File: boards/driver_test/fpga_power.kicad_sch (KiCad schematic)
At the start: 34 parts, among them J2 Barrel_Jack_Switch, J3 Conn_01x24, J4 Conn_01x24, Q4 IRF7413, U2 74LVC245, U3 JTE0624D05, U4 ADP151-3.3, U5 LTC4231-1, U6 74HC4514, U7 74LVC2G04

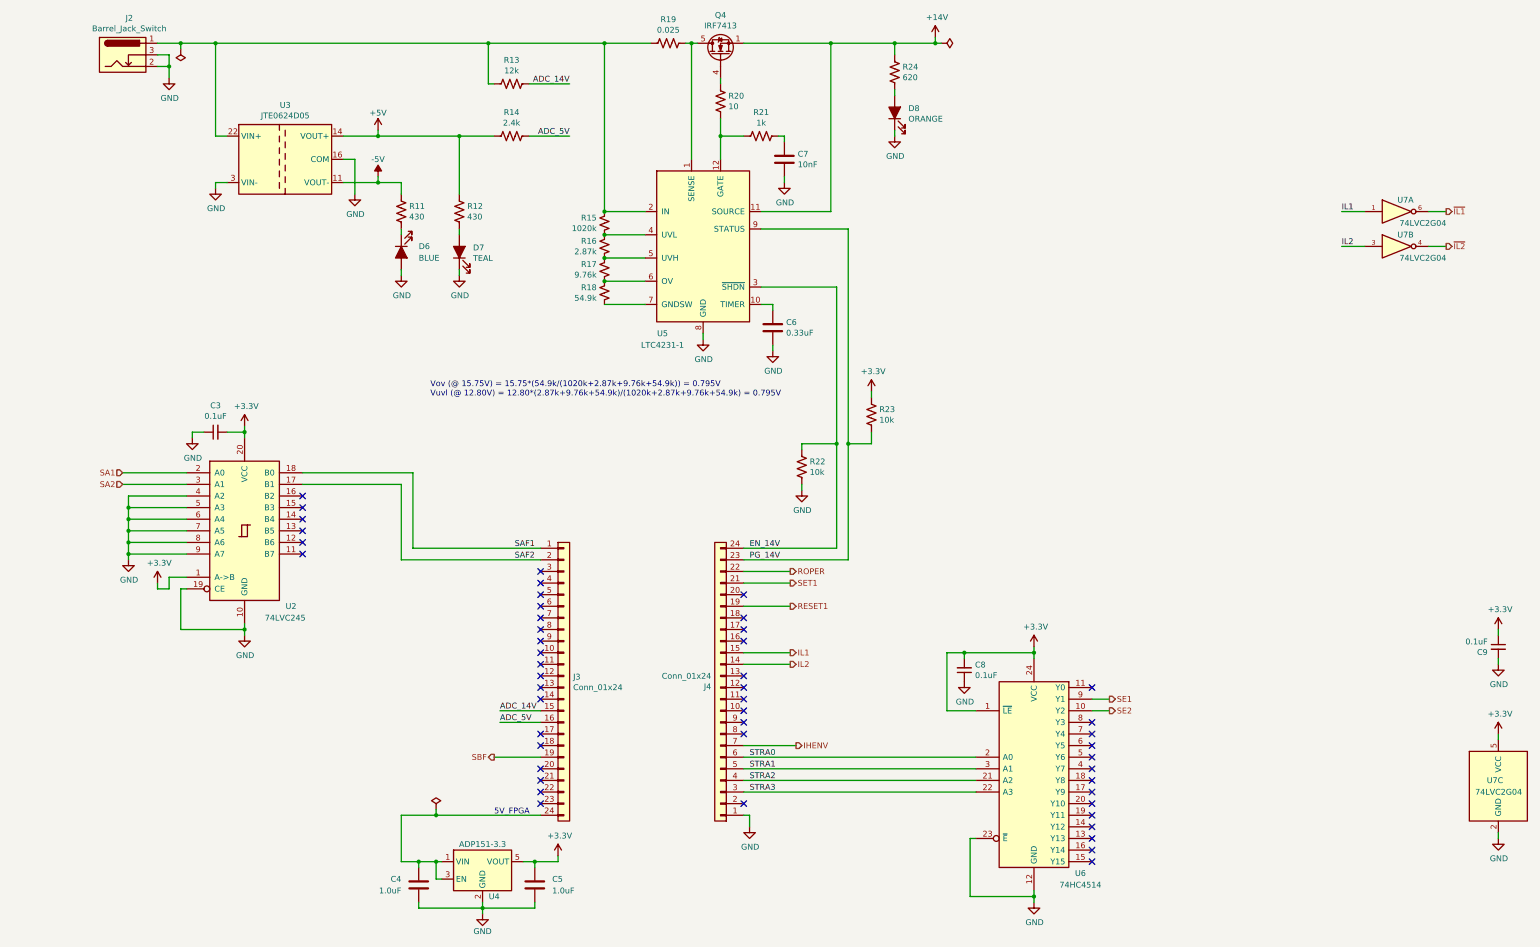
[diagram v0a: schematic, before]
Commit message: Driver test: completed much of the preliminary layout.
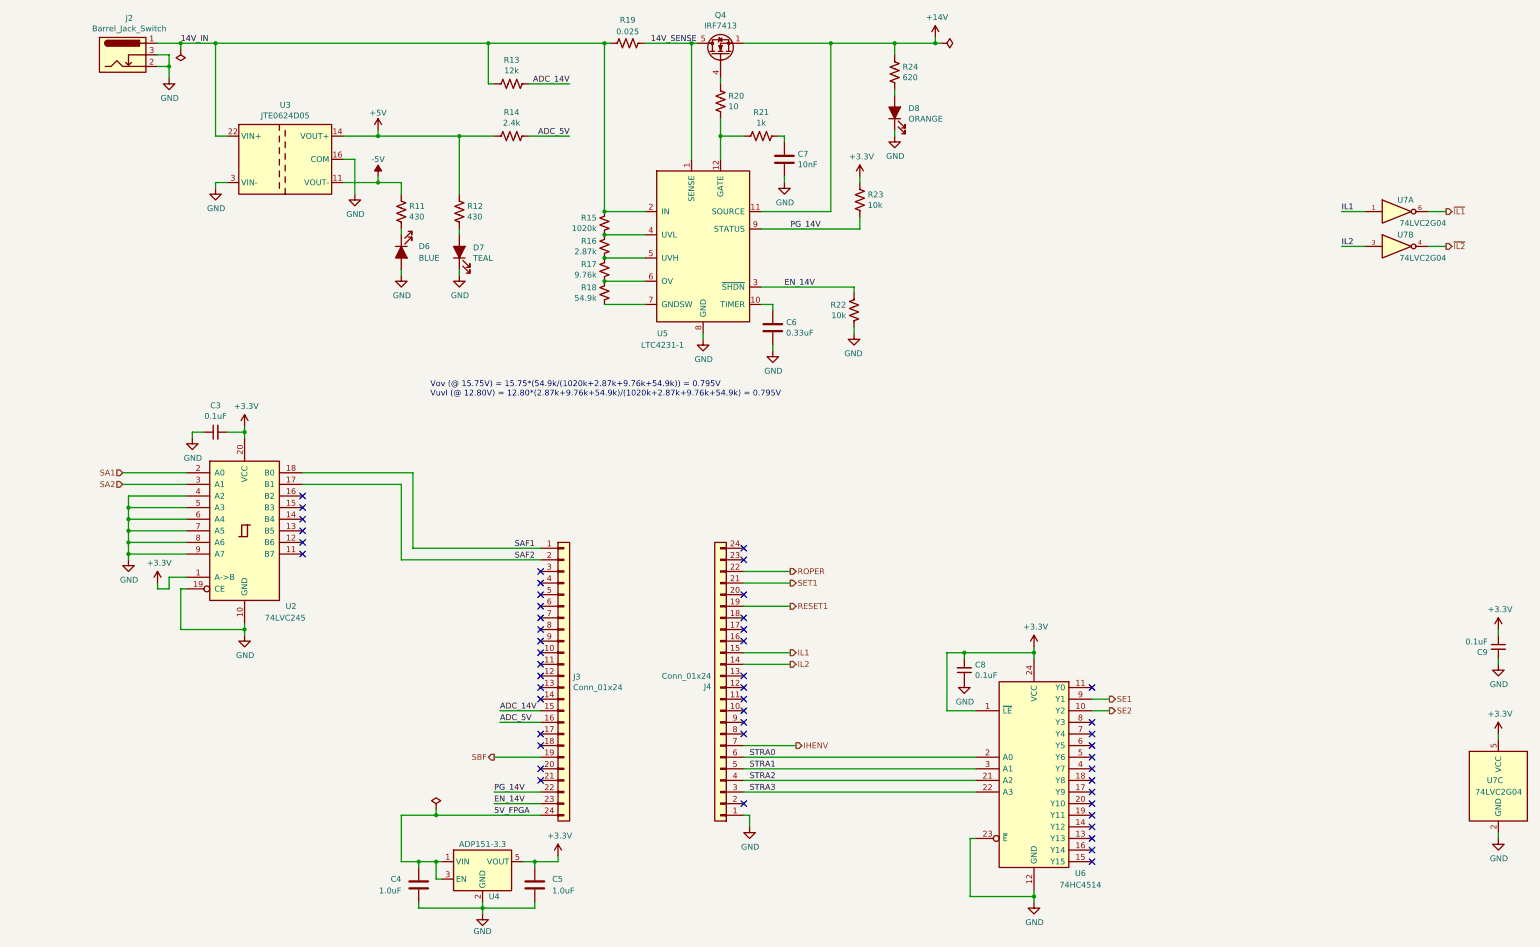
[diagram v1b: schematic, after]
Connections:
- net EN_14V: now also J3.23 (Pin_23); no longer J4.24 (Pin_24)
- net PG_14V: now also J3.22 (Pin_22); no longer J4.23 (Pin_23)
- net 14V_SENSE: now reaches Q4.5 (D), Q4.6 (D), Q4.7 (D), Q4.8 (D), U5.1 (SENSE)
- net 14V_SENSE: now also R19.2; no longer R19.1
- net 14V_IN: now reaches J2.1, R13.2, R15.2, U3.22 (VIN+), U3.23 (VIN+), U5.2 (IN)
- net 14V_IN: now also R19.1; no longer R19.2
- net 5V_FPGA: now reaches C4.2, J3.24 (Pin_24), U4.1 (VIN), U4.3 (EN)
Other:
- note removed: "5V_FPGA"
- moved on the sheet: R19, R22, R23

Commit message: Driver test: finished up board layout
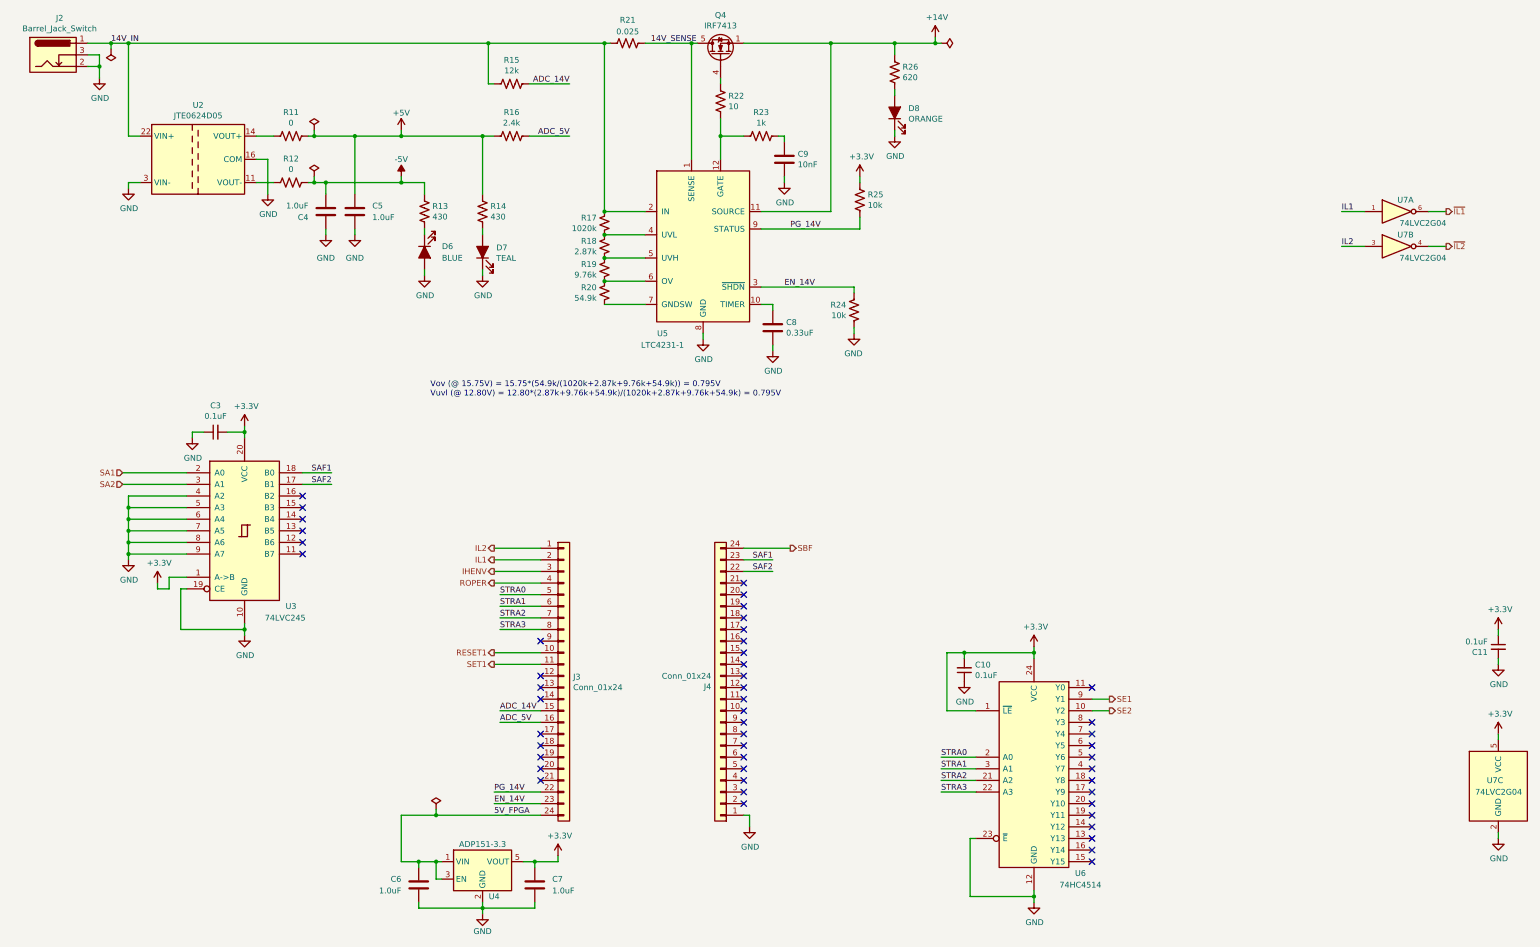
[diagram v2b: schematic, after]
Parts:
- added C4, C5: 1.0uF, Capacitor_SMD:C_0805_2012Metric, symbol Device:C
- added R11, R12: 0, Resistor_SMD:R_0805_2012Metric, symbol Device:R_US
- Q4: footprint Package_SO:SO-8_3.9x4.9mm_P1.27mm -> Package_SO:SOIC-8_3.9x4.9mm_P1.27mm
- renumbered C8 to C10, C9 to C11, C4 to C6, C5 to C7, C6 to C8, C7 to C9, R11 to R13, R12 to R14, R13 to R15, R14 to R16, R15 to R17, R16 to R18, R17 to R19, R18 to R20, R19 to R21, R20 to R22, R21 to R23, R22 to R24, R23 to R25, R24 to R26, U3 to U2, U2 to U3
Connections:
- net +5V: now also C5.1, R11.1; no longer U2.14 (VOUT+)
- net -5V: now also C4.2, R12.1; no longer U2.11 (VOUT-)
- net GND: now also C4.1, C5.2
- net IHENV: now also J3.3 (Pin_3); no longer J4.7 (Pin_7)
- net IL1: now also J3.2 (Pin_2); no longer J4.15 (Pin_15)
- net IL2: now also J3.1 (Pin_1); no longer J4.14 (Pin_14)
- net RESET1: now also J3.10 (Pin_10); no longer J4.19 (Pin_19)
- net ROPER: now also J3.4 (Pin_4); no longer J4.22 (Pin_22)
- net SAF1: now also J4.23 (Pin_23); no longer J3.1 (Pin_1)
- net SAF2: now also J4.22 (Pin_22); no longer J3.2 (Pin_2)
- net SBF: now also J4.24 (Pin_24); no longer J3.19 (Pin_19)
- net SET1: now also J3.11 (Pin_11); no longer J4.21 (Pin_21)
- net STRA0: now also J3.5 (Pin_5); no longer J4.6 (Pin_6)
- net STRA1: now also J3.6 (Pin_6); no longer J4.5 (Pin_5)
- net STRA2: now also J3.7 (Pin_7); no longer J4.4 (Pin_4)
- net STRA3: now also J3.8 (Pin_8); no longer J4.3 (Pin_3)
- new net: R12.2, U2.11 (VOUT-)
- new net: R11.2, U2.14 (VOUT+)
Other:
- moved on the sheet: D6, D7, J2, R13, R14, U2

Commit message: Driver test: some updates to component values based on new documentation
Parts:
- C10, C11, C3: Rating (none) -> 50V; Tolerance (none) -> 10%
- C6, C7: Digikey (none) -> https://www.digikey.com/en/products/detail/samsung-electro-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; Rating (none) -> 25V; Tolerance (none) -> 10%
- C8: value 0.33uF -> 100pF; Rating (none) -> 50V; Tolerance (none) -> 10%
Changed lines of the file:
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@@
+      (effects (font (size 1.27 1.27)) hide)
+    )
+    (property "Rating" "50V" (id 4) (at 81.28 121.92 0)
+      (effects (font (size 1.27 1.27)) hide)
+    )
+    (property "Tolerance" "10%" (id 5) (at 81.28 121.92 0)
       (effects (font (size 1.27 1.27)) hide)
     )
@@
     )
     (property "Datasheet" "~" (id 3) (at 245.11 173.99 0)
+      (effects (font (size 1.27 1.27)) hide)
+    )
+    (property "Rating" "50V" (id 4) (at 245.11 173.99 0)
+      (effects (font (size 1.27 1.27)) hide)
+    )
+    (property "Tolerance" "10%" (id 5) (at 245.11 173.99 0)
       (effects (font (size 1.27 1.27)) hide)
     )
@@
       (effects (font (size 1.27 1.27)) (justify left))
     )
-    (property "Value" "0.33uF" (id 1) (at 206.121 100.203 0)
+    (property "Value" "100pF" (id 1) (at 206.121 100.203 0)
       (effects (font (size 1.27 1.27)) (justify left))
     )
@@
     )
     (property "Datasheet" "~" (id 3) (at 203.2 99.06 0)
+      (effects (font (size 1.27 1.27)) hide)
+    )
+    (property "Rating" "50V" (id 4) (at 203.2 99.06 0)
+      (effects (font (size 1.27 1.27)) hide)
+    )
+    (property "Tolerance" "10%" (id 5) (at 203.2 99.06 0)
       (effects (font (size 1.27 1.27)) hide)
     )
@@
     )
     (property "Datasheet" "~" (id 3) (at 361.95 168.91 0)
+      (effects (font (size 1.27 1.27)) hide)
+    )
+    (property "Rating" "50V" (id 4) (at 361.95 168.91 0)
+      (effects (font (size 1.27 1.27)) hide)
+    )
+    (property "Tolerance" "10%" (id 5) (at 361.95 168.91 0)
       (effects (font (size 1.27 1.27)) hide)
     )
@@
       (effects (font (size 1.27 1.27)) hide)
     )
+    (property "Digikey" "https://www.digikey.com/en/products/detail/samsung-electro-mechanics/CL10B105KP8NNNC/3887604" (id 4) (at 125.73 220.98 0)
+      (effects (font (size 1.27 1.27)) hide)
+    )
+    (property "Rating" "25V" (id 5) (at 125.73 220.98 0)
+      (effects (font (size 1.27 1.27)) hide)
+    )
+    (property "Tolerance" "10%" (id 6) (at 125.73 220.98 0)
+      (effects (font (size 1.27 1.27)) hide)
+    )
     (pin "1")
     (pin "2")
@@
       (effects (font (size 1.27 1.27)) hide)
     )
+    (property "Digikey" "https://www.digikey.com/en/products/detail/samsung-electro-mechanics/CL10B105KP8NNNC/3887604" (id 4) (at 151.13 220.98 0)
+      (effects (font (size 1.27 1.27)) hide)
+    )
+    (property "Rating" "25V" (id 5) (at 151.13 220.98 0)
+      (effects (font (size 1.27 1.27)) hide)
+    )
+    (property "Tolerance" "10%" (id 6) (at 151.13 220.98 0)
+      (effects (font (size 1.27 1.27)) hide)
+    )

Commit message: Driver test: some minor component value changes
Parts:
- C9: value 10nF -> 0.01uF
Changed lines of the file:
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@@
       (effects (font (size 1.27 1.27)) (justify left))
     )
-    (property "Value" "10nF" (id 1) (at 208.661 63.373 0)
+    (property "Value" "0.01uF" (id 1) (at 208.661 63.373 0)
       (effects (font (size 1.27 1.27)) (justify left))
     )

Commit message: Driver test: dropped BPLSSW LED brightness by bumping its resistor up to 1k
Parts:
- R26: value 620 -> 1k
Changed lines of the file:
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@@
       (effects (font (size 1.27 1.27)) (justify left))
     )
-    (property "Value" "620" (id 1) (at 231.5972 44.323 0)
+    (property "Value" "1k" (id 1) (at 231.5972 44.323 0)
       (effects (font (size 1.27 1.27)) (justify left))
     )
